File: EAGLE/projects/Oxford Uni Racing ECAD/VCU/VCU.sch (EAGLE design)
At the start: 53 parts, among them IC1 AD711N, IC2 LM2901D, IC3 4081D, J1 PWR_CAN, J2 ASS+BRAKE_LIGHTS, J3 MC_LEFT, J4 MC_RIGHT, J5 BR_PRESS, J6 LEFT_COOLING_SENSOR, J8 RIGHT_COOLING_SENSOR, K1 RT444012, T2 BT169, U1 REF3040AIDBZT, X2 D-SUB9-H2M09ST

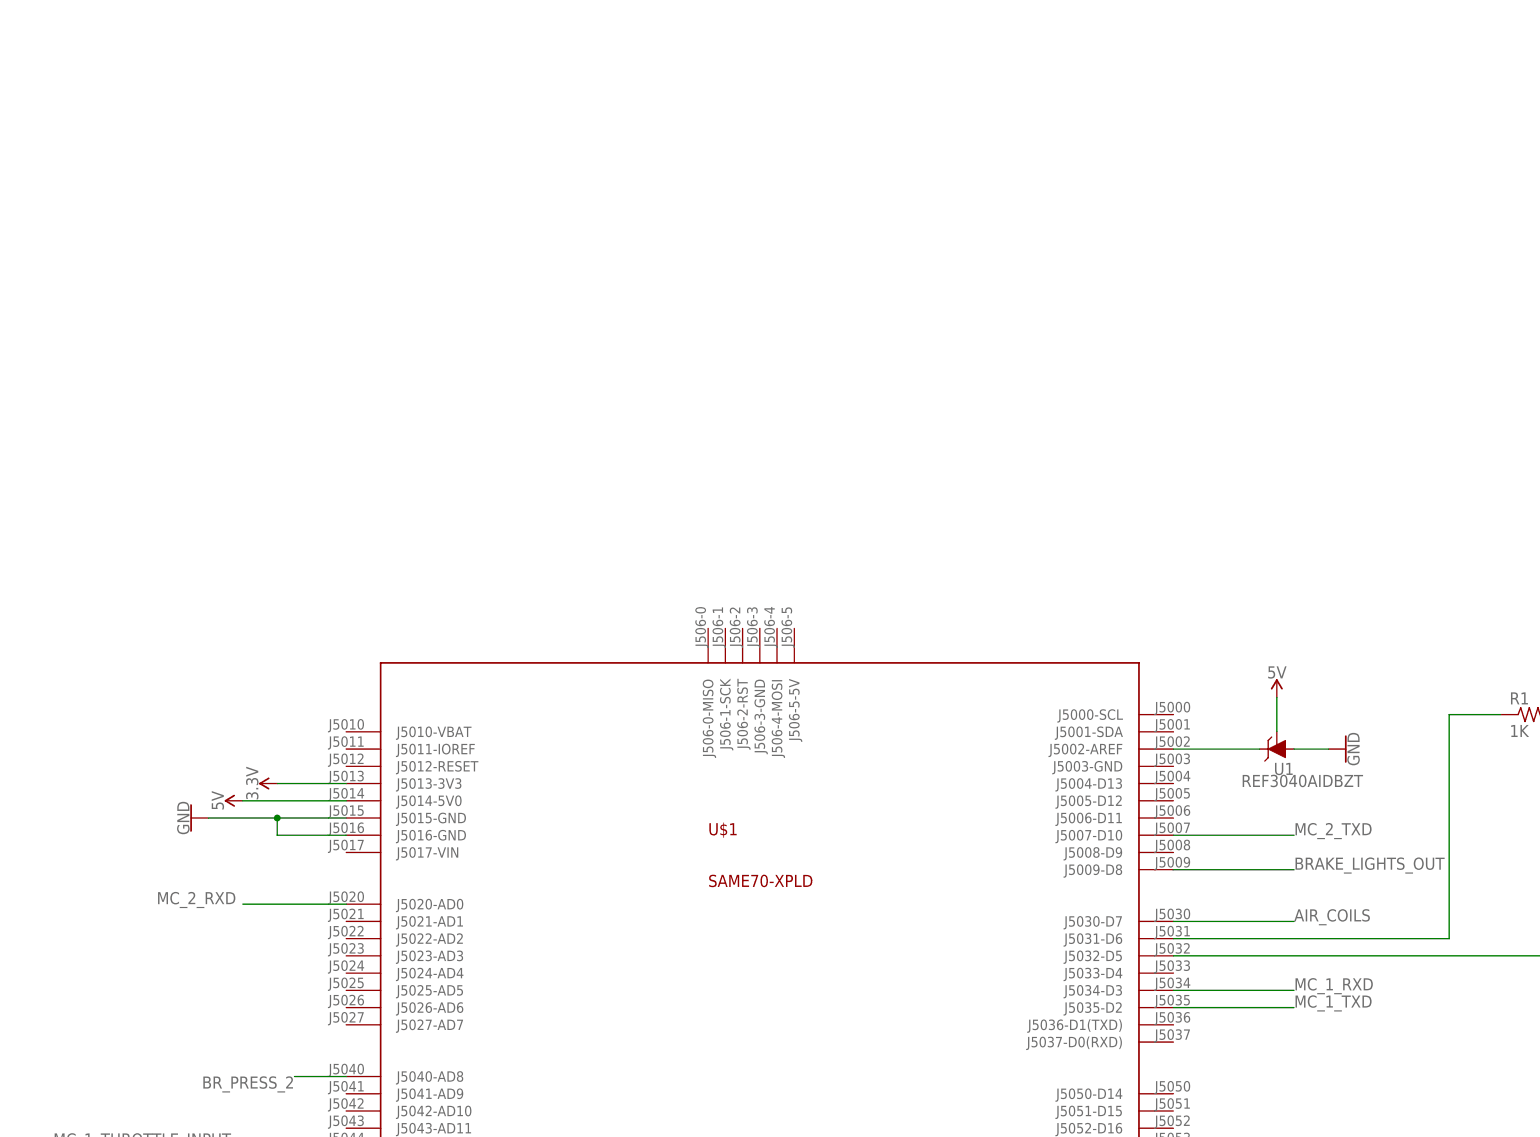
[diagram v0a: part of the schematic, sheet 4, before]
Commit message: added RS232 chip to the vcu
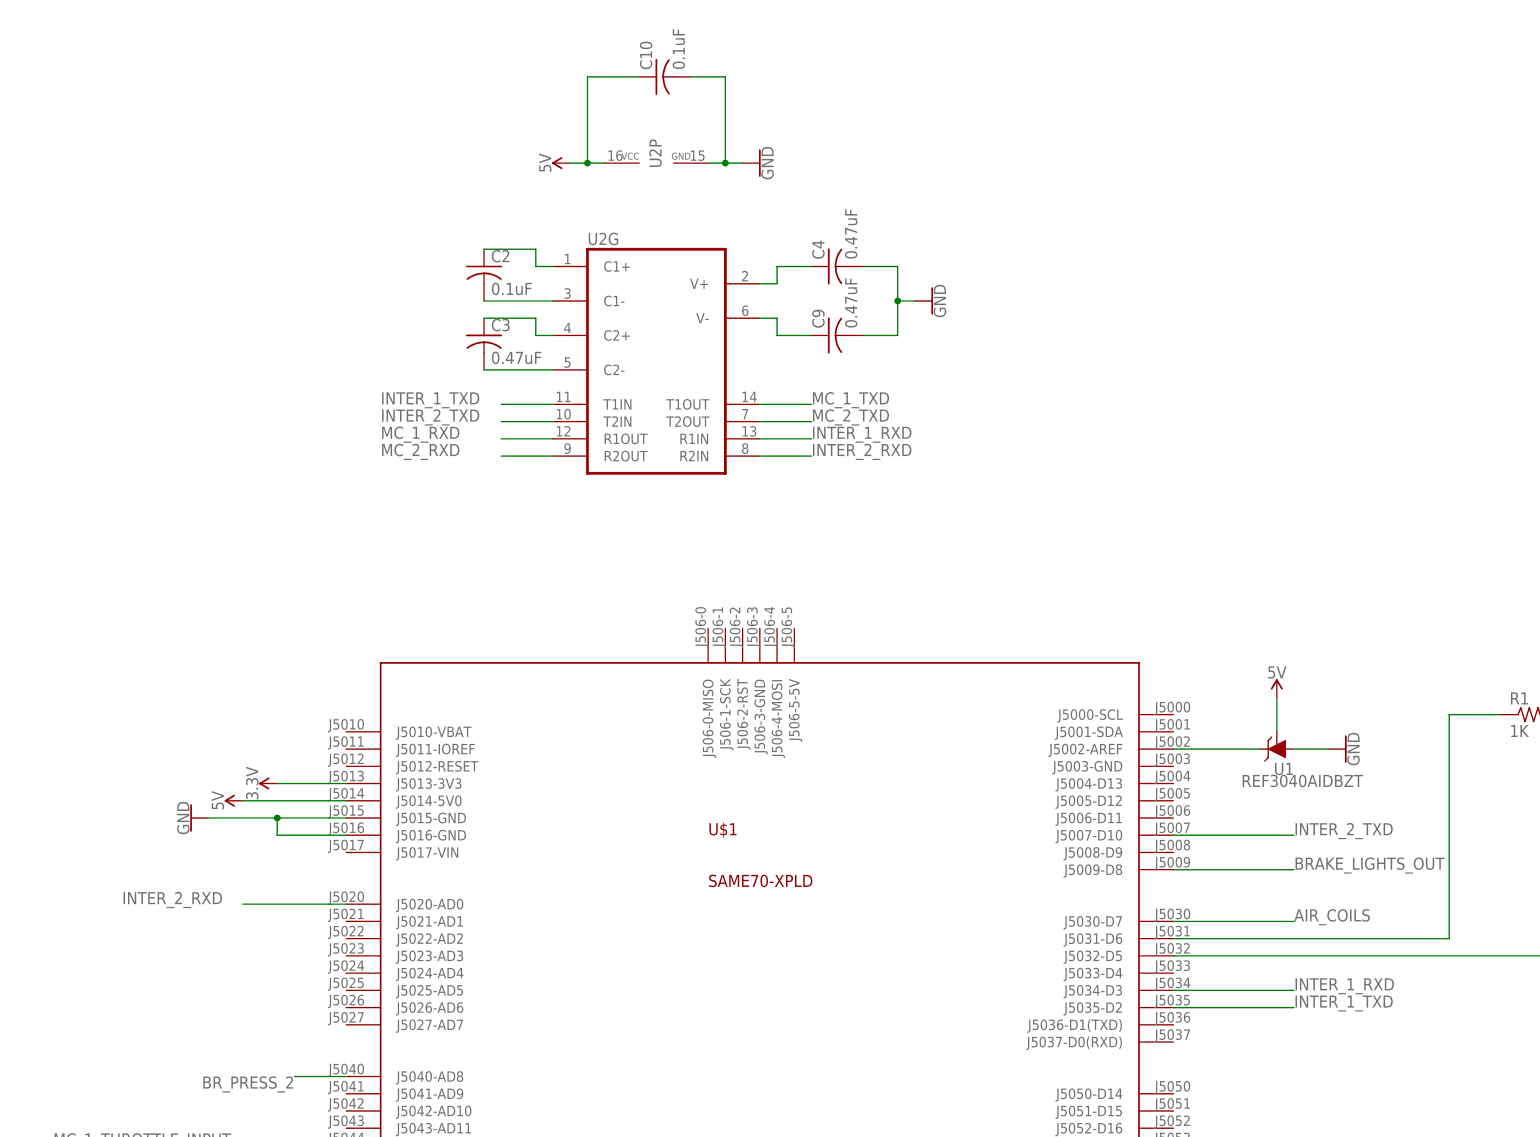
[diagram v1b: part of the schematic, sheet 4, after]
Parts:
- added C10, C2: 0.1uF, adafruit:C-US025-024X044
- added C3, C4, C9: 0.47uF, adafruit:C-US025-024X044
- added U2: (no value), m-pad-2.1:MAX3232S
- R1, R2: device adafruit:R-US_0204/7 -> adafruit:R-US_R0805
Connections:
- new net INTER_1_RXD: U$1.J5034-D3, U2G.R1IN
- new net INTER_1_TXD: U$1.J5035-D2, U2G.T1IN
- new net INTER_2_RXD: U$1.J5020-AD0, U2G.R2IN
- new net INTER_2_TXD: U$1.J5007-D10, U2G.T2IN
- new net N$10: C2.2, U2G.C1-
- new net N$11: C2.1, U2G.C1+
- new net N$14: C4.1, U2G.V+
- new net N$15: C9.1, U2G.V-
- new net N$8: C3.2, U2G.C2-
- new net N$9: C3.1, U2G.C2+
- net 5V: now also C10.1, U2P.VCC
- net GND: now also C10.2, C4.2, C9.2, U2P.GND
- net MC_1_RXD: now also U2G.R1OUT; no longer U$1.J5034-D3
- net MC_1_TXD: now also U2G.T1OUT; no longer U$1.J5035-D2
- net MC_2_RXD: now also U2G.R2OUT; no longer U$1.J5020-AD0
- net MC_2_TXD: now also U2G.T2OUT; no longer U$1.J5007-D10

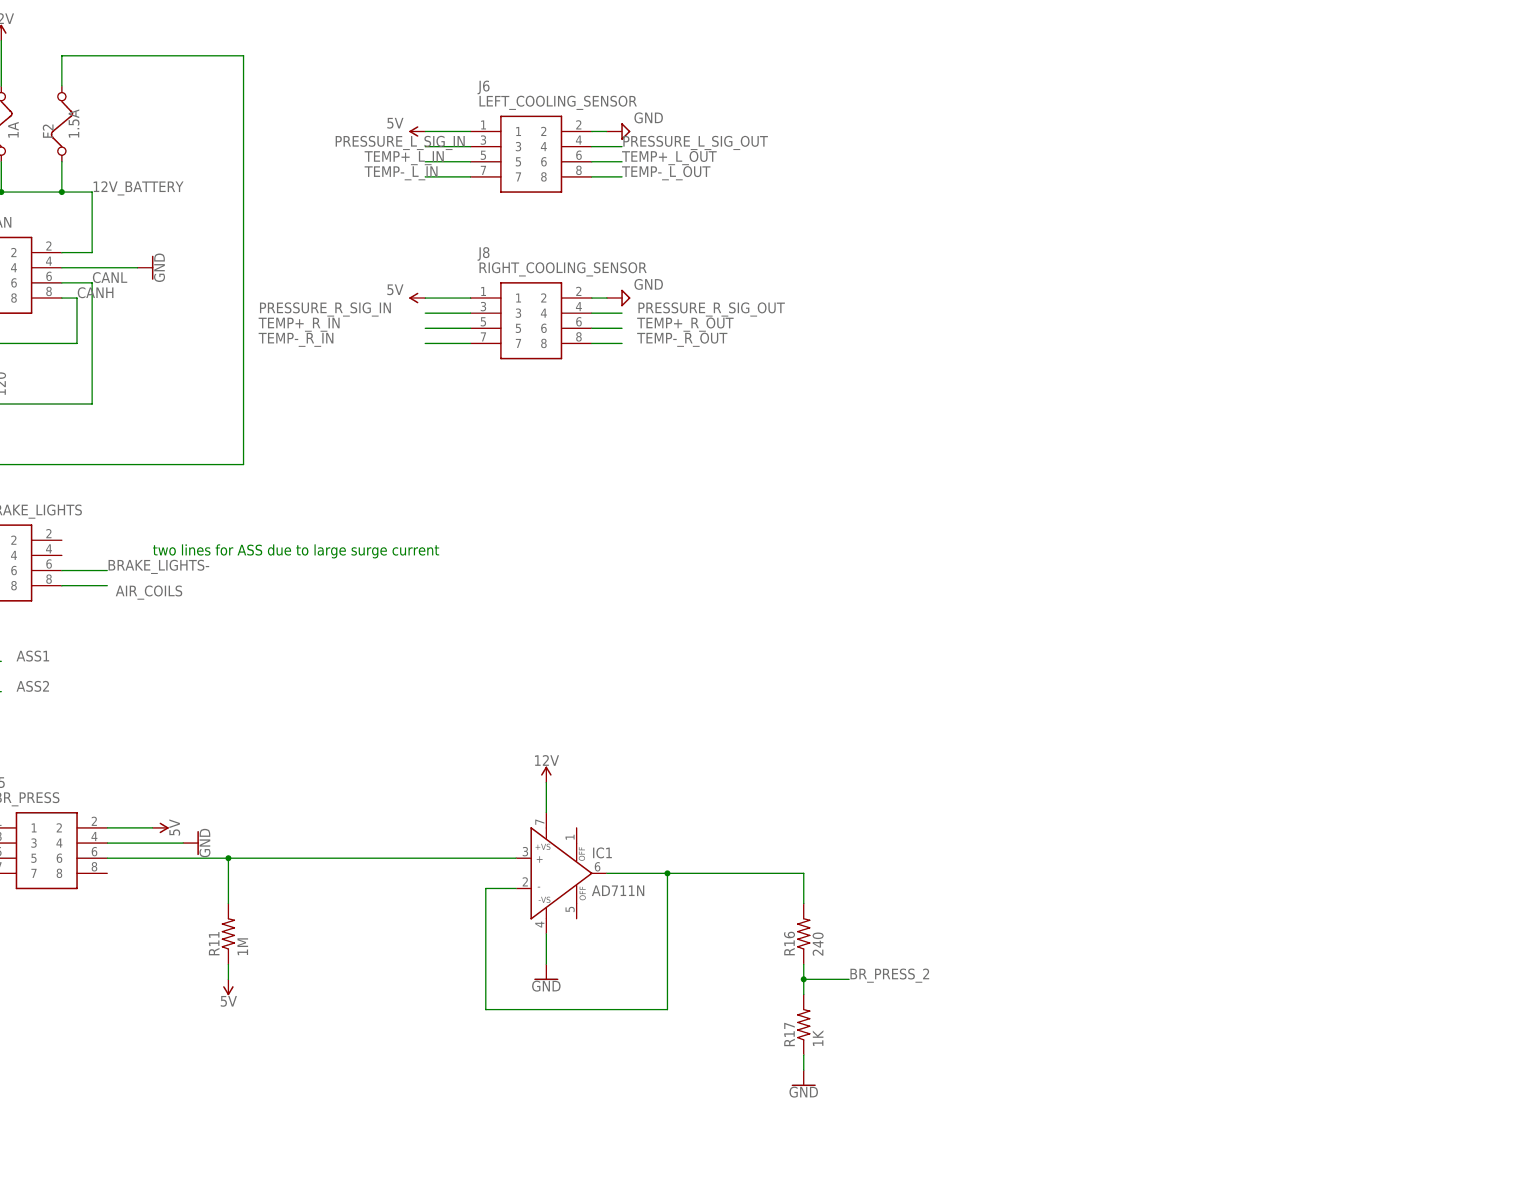
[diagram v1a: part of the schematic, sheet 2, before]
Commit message: added op-amps to pressire sensors and resistors to temp sensors on the vcu
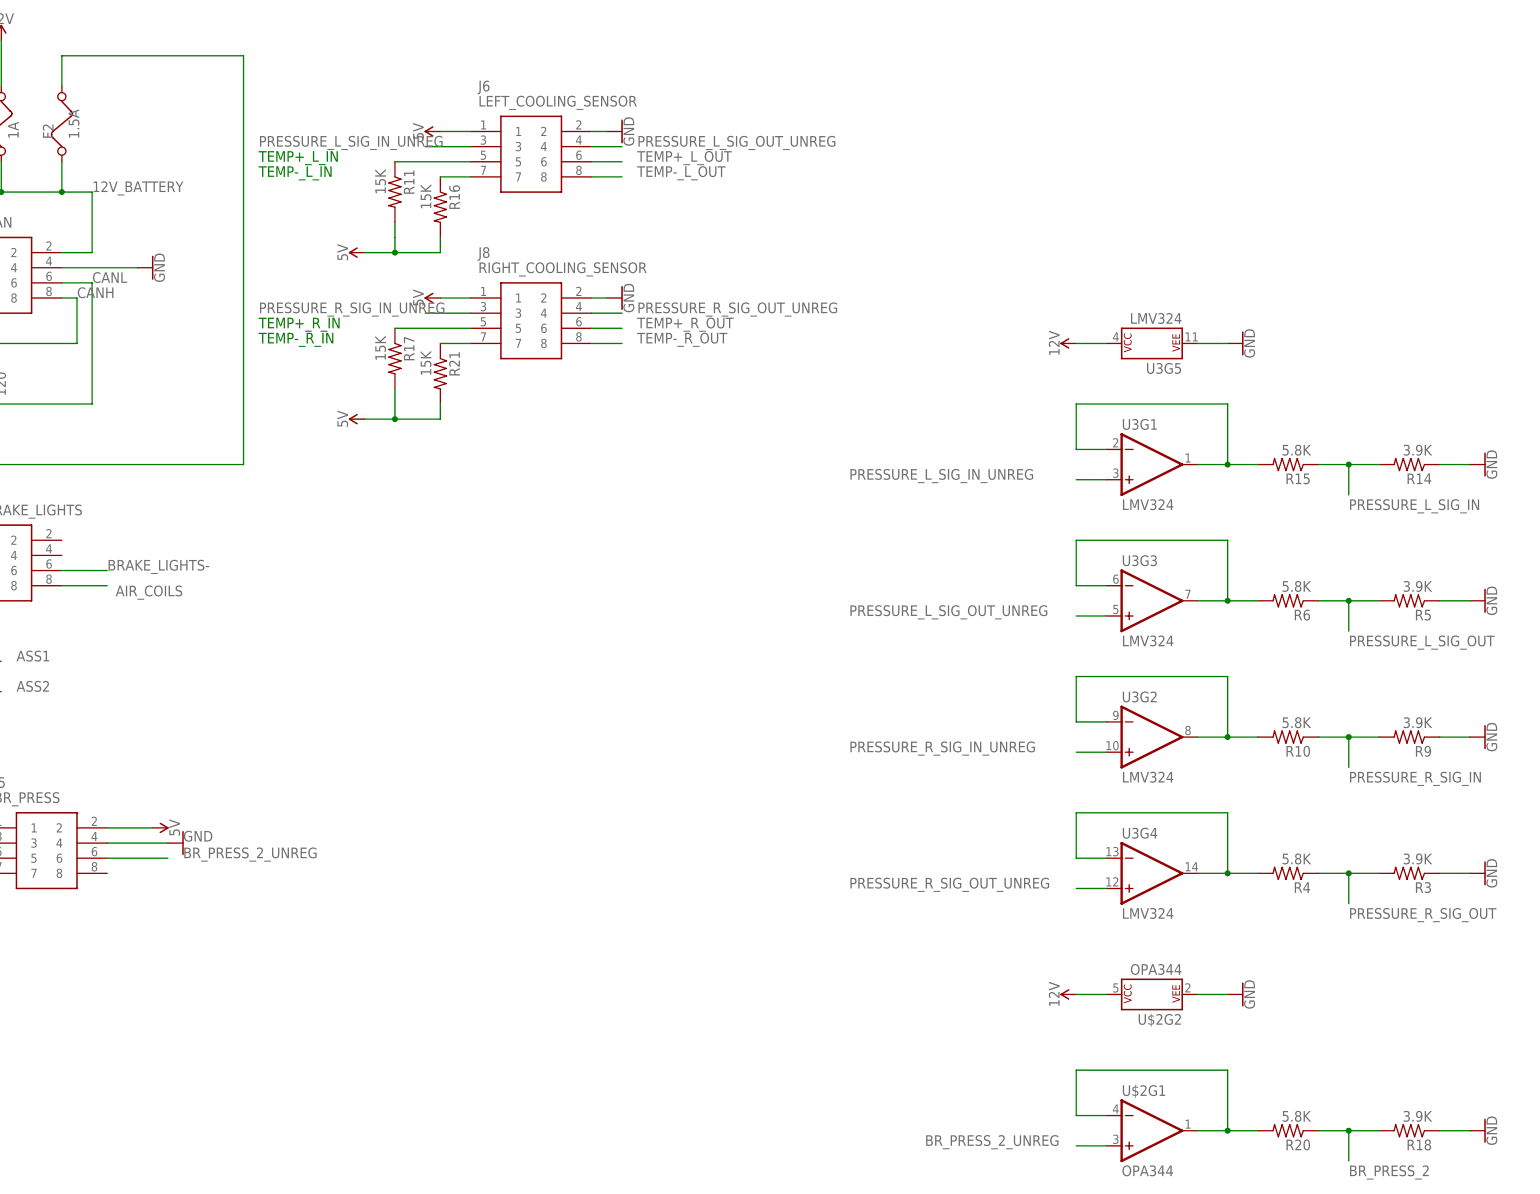
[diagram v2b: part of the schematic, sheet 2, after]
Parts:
- removed IC1: AD711N, analog-devices:AD711N
- added R10, R15, R20, R4, R6: 5.8K, adafruit:R-US_R0805
- added R14, R18, R3, R5, R9: 3.9K, adafruit:R-US_R0805
- added R21: 15K, adafruit:R-US_R0805
- added U$2: OPA344, SparkFun-IC-Amplifiers:OPA344
- added U3: LMV324, SparkFun-IC-Amplifiers:LMV324
- R11: value 1M -> 15K; device adafruit:R-US_0204/7 -> adafruit:R-US_R0805
- R16: value 240 -> 15K; device adafruit:R-US_0204/7 -> adafruit:R-US_R0805
- R17: value 1K -> 15K; device adafruit:R-US_0204/7 -> adafruit:R-US_R0805
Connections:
- removed net N$23: IC1.IN-, IC1.OUT, R16.2
- removed net N$27: IC1.IN+, J5.6, R11.2
- removed net TEMP+_L_IN: J6.5
- removed net TEMP+_R_IN: J8.5
- removed net TEMP-_L_IN: J6.7
- removed net TEMP-_R_IN: J8.7
- new net BR_PRESS_2_UNREG: J5.6, U$2G1.+IN
- new net N$13: R4.2, U3G4.-IN, U3G4.OUT
- new net N$16: J8.5, R17.1
- new net N$17: R6.2, U3G3.-IN, U3G3.OUT
- new net N$18: J8.7, R21.1
- new net N$19: R10.2, U3G2.-IN, U3G2.OUT
- new net N$20: J6.7, R16.1
- new net N$21: R15.2, U3G1.-IN, U3G1.OUT
- new net N$22: J6.5, R11.1
- new net N$24: R20.2, U$2G1.-IN, U$2G1.OUT
- new net PRESSURE_L_SIG_IN_UNREG: J6.3, U3G1.+IN
- new net PRESSURE_L_SIG_OUT_UNREG: J6.4, U3G3.+IN
- new net PRESSURE_R_SIG_IN_UNREG: J8.3, U3G2.+IN
- new net PRESSURE_R_SIG_OUT_UNREG: J8.4, U3G4.+IN
- net 12V: now also U$2G2.P$V+, U3G5.P$V+; no longer IC1.+VS
- net 5V: now also R11.2, R16.2, R17.2, R21.2; no longer R11.1
- net BR_PRESS_2: now also R18.2, R20.1; no longer R16.1, R17.2
- net GND: now also R14.1, R18.1, R3.1, R5.1, R9.1, U$2G2.P$V-, U3G5.P$V-; no longer IC1.-VS, R17.1
- net PRESSURE_L_SIG_IN: now also R14.2, R15.1; no longer J6.3
- net PRESSURE_L_SIG_OUT: now also R5.2, R6.1; no longer J6.4
- net PRESSURE_R_SIG_IN: now also R10.1, R9.2; no longer J8.3
- net PRESSURE_R_SIG_OUT: now also R3.2, R4.1; no longer J8.4
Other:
- note added: "TEMP+_L_IN"
- note added: "TEMP+_R_IN"
- note added: "TEMP-_L_IN"
- note added: "TEMP-_R_IN"
- note removed: "two lines for ASS due to large surge current"
- moved on the sheet: R11, R16, R17
